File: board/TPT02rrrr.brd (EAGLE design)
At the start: 28.4 x 28.4 mm, 16 parts, among them SW4 SW_SLIDECUS12B, U1 MOD_CYBLE014008-00, U2 REG_TPS61221

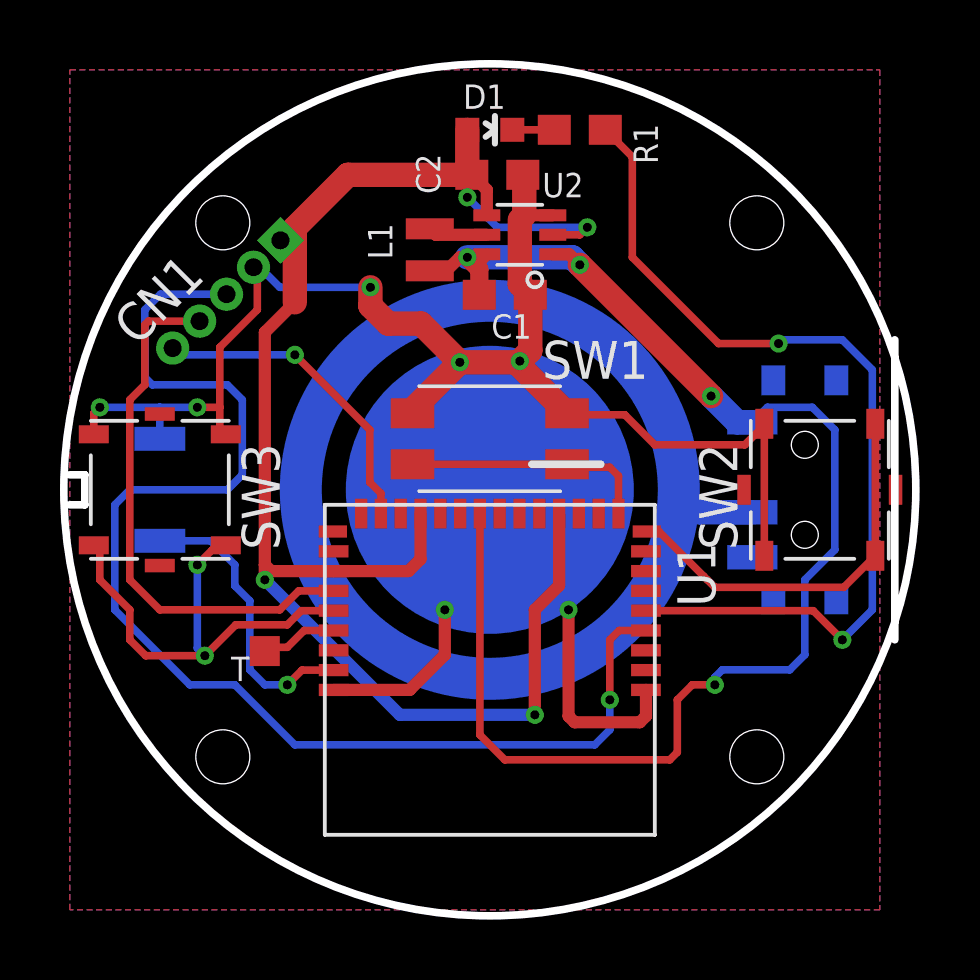
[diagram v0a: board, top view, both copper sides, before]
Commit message: 両側のタクトスイッチのGND端子が基板端にかかるため削除
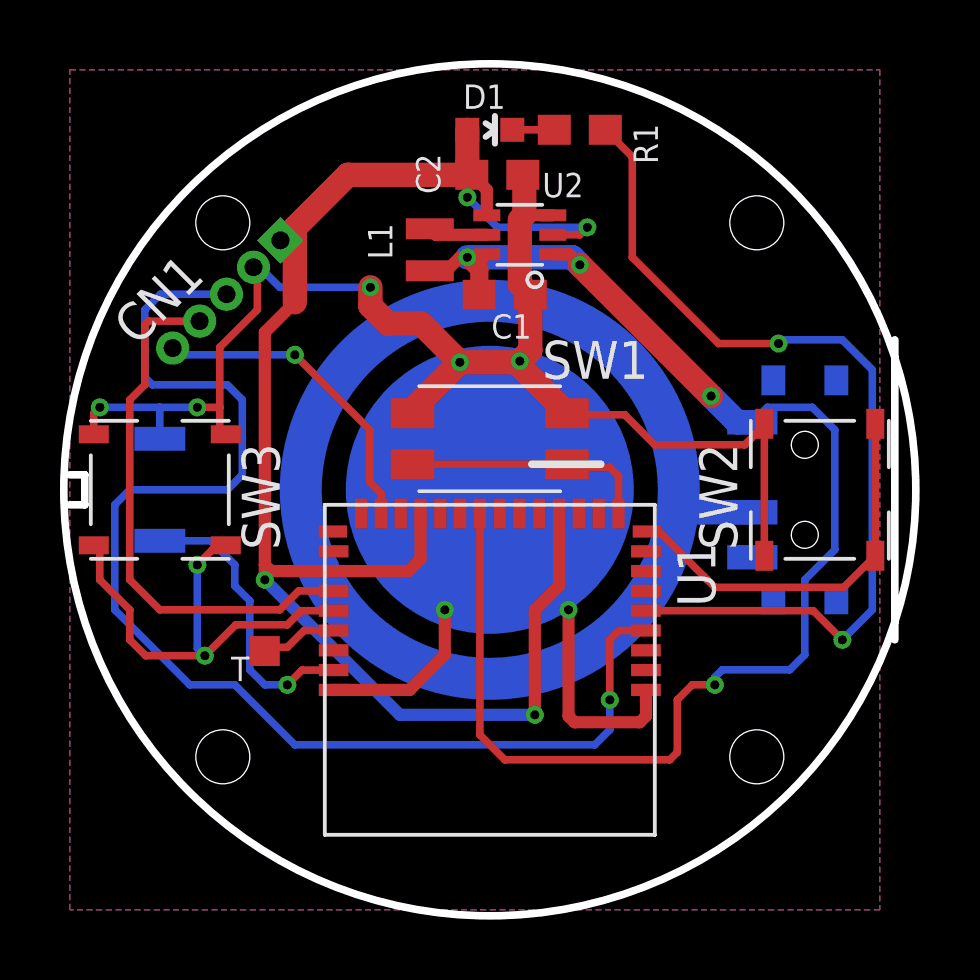
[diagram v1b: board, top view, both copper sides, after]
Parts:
- SW2, SW3: device akita:SW_EVQPLBA08 -> akita:SW_EVQPLBA08_NOGND
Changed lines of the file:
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@@
 <setting verticaltext="up"/>
 </settings>
-<grid distance="1" unitdist="mm" unit="mm" style="lines" multiple="1" display="yes" altdistance="0.5" altunitdist="mm" altunit="mm"/>
+<grid distance="1.27" unitdist="mm" unit="mm" style="lines" multiple="1" display="yes" altdistance="0.5" altunitdist="mm" altunit="mm"/>
 <layers>
 <layer number="1" name="Top" color="4" fill="1" visible="yes" active="yes"/>
@@
 <attribute name="VALUE" x="17.5" y="19.7" size="1.27" layer="27" rot="R180"/>
 </element>
-<element name="SW3" library="akita" package="SW_EVQPLBA08" value="" x="4" y="15" smashed="yes" rot="R90">
+<element name="SW3" library="akita" package="SW_EVQPLBA08_NOGND" value="" x="4" y="15" smashed="yes" rot="R90">
 <attribute name="NAME" x="8" y="13" size="1.27" layer="25" rot="R90"/>
 <attribute name="VALUE" x="8" y="12.5" size="1.27" layer="27" rot="R90"/>
 </element>
-<element name="SW2" library="akita" package="SW_EVQPLBA08" value="" x="26" y="15" smashed="yes" rot="R180">
+<element name="SW2" library="akita" package="SW_EVQPLBA08_NOGND" value="" x="26" y="15" smashed="yes" rot="R180">
 <attribute name="NAME" x="23.25" y="13" size="1.27" layer="25" rot="R90"/>
 <attribute name="VALUE" x="28.5" y="19" size="1.27" layer="27" rot="R180"/>
